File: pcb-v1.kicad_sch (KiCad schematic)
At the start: 0 parts

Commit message: add arduino due symbol
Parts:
- added A1: Arduino_Due_Shield, PCM_arduino-library:Arduino_Due_Shield, symbol arduino-library-wit:Arduino_Due_Shield
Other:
- company: (none) -> Control Data (Thailand) LTD.
- title: (none) -> IOBox

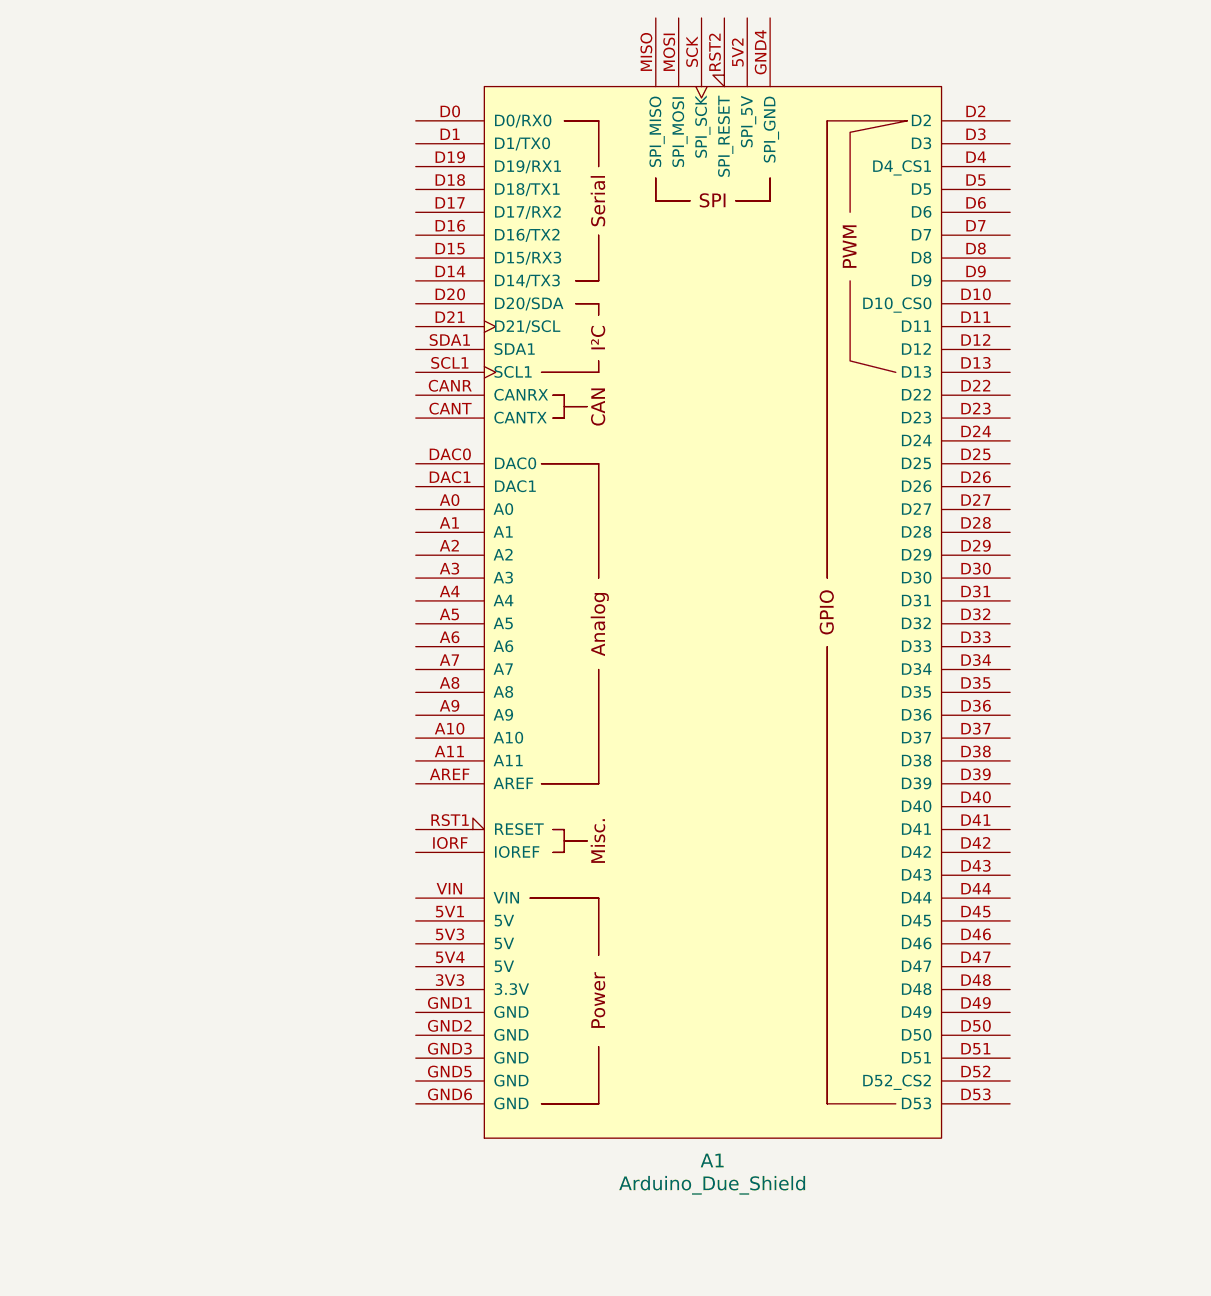
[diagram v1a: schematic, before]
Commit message: add voltage sensor pin
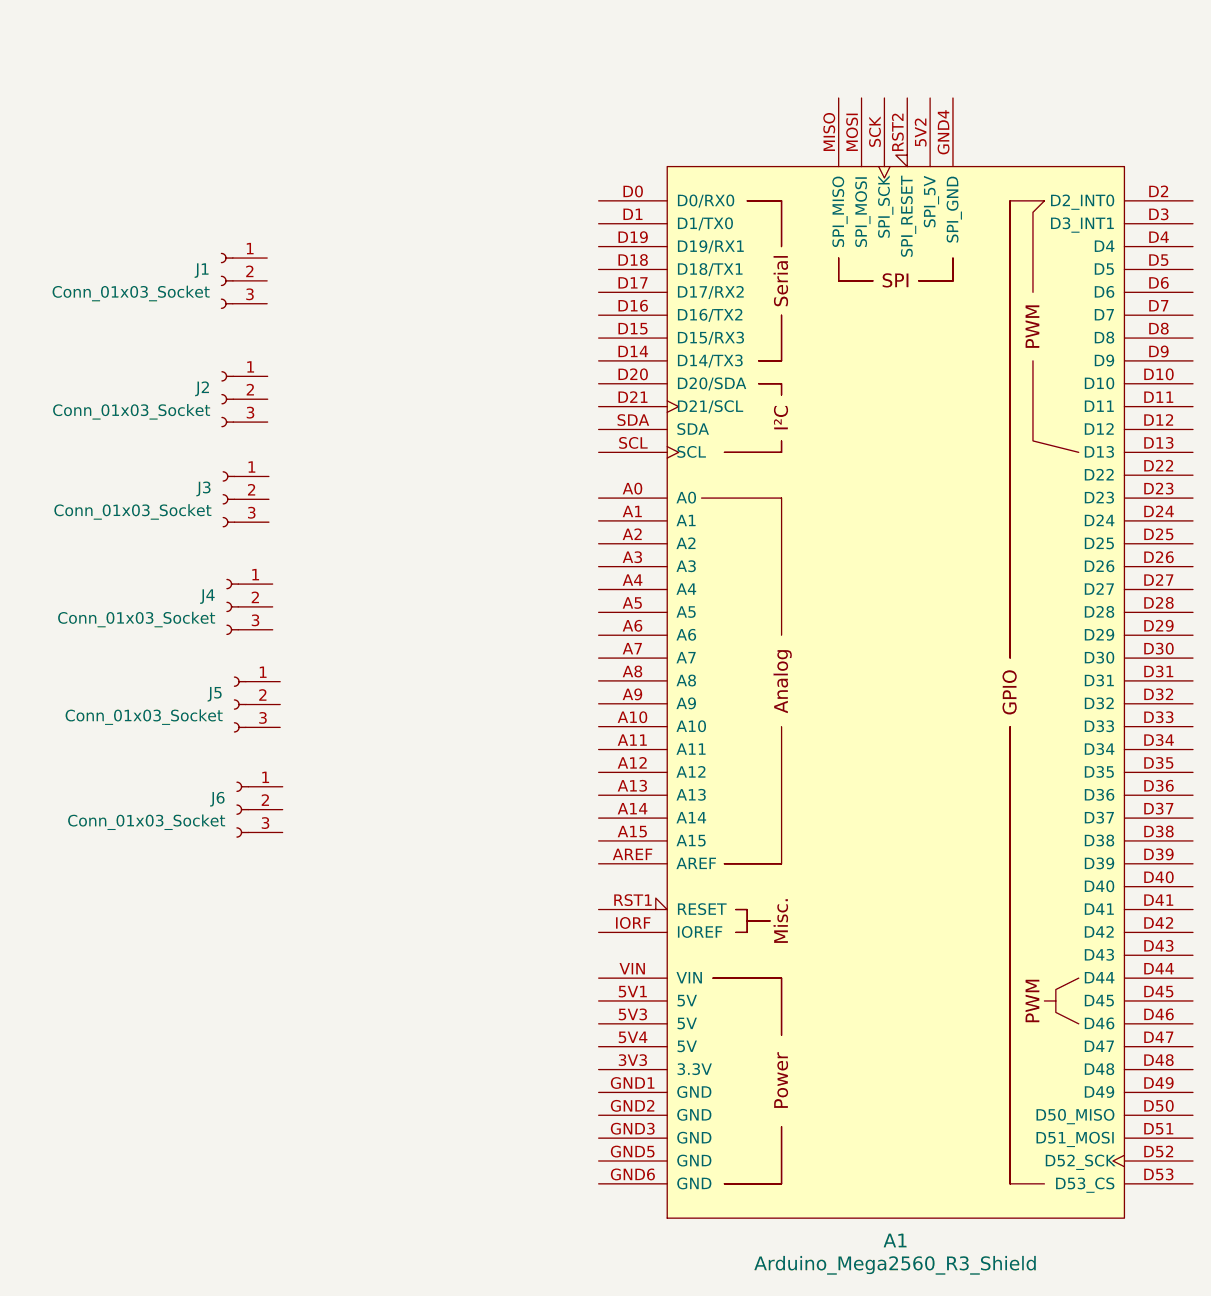
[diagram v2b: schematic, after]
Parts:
- removed A1: Arduino_Due_Shield, PCM_arduino-library:Arduino_Due_Shield, symbol arduino-library-wit:Arduino_Due_Shield
- added A1: Arduino_Mega2560_R3_Shield, arduino-library:Arduino_Mega2560_R3_Shield, symbol arduino-library-kidcad:Arduino_Mega2560_R3_Shield
- added J1, J2, J3, J4, J5, J6: Conn_01x03_Socket, Connector_PinSocket_2.54mm:PinSocket_1x03_P2.54mm_Vertical, symbol Connector:Conn_01x03_Socket

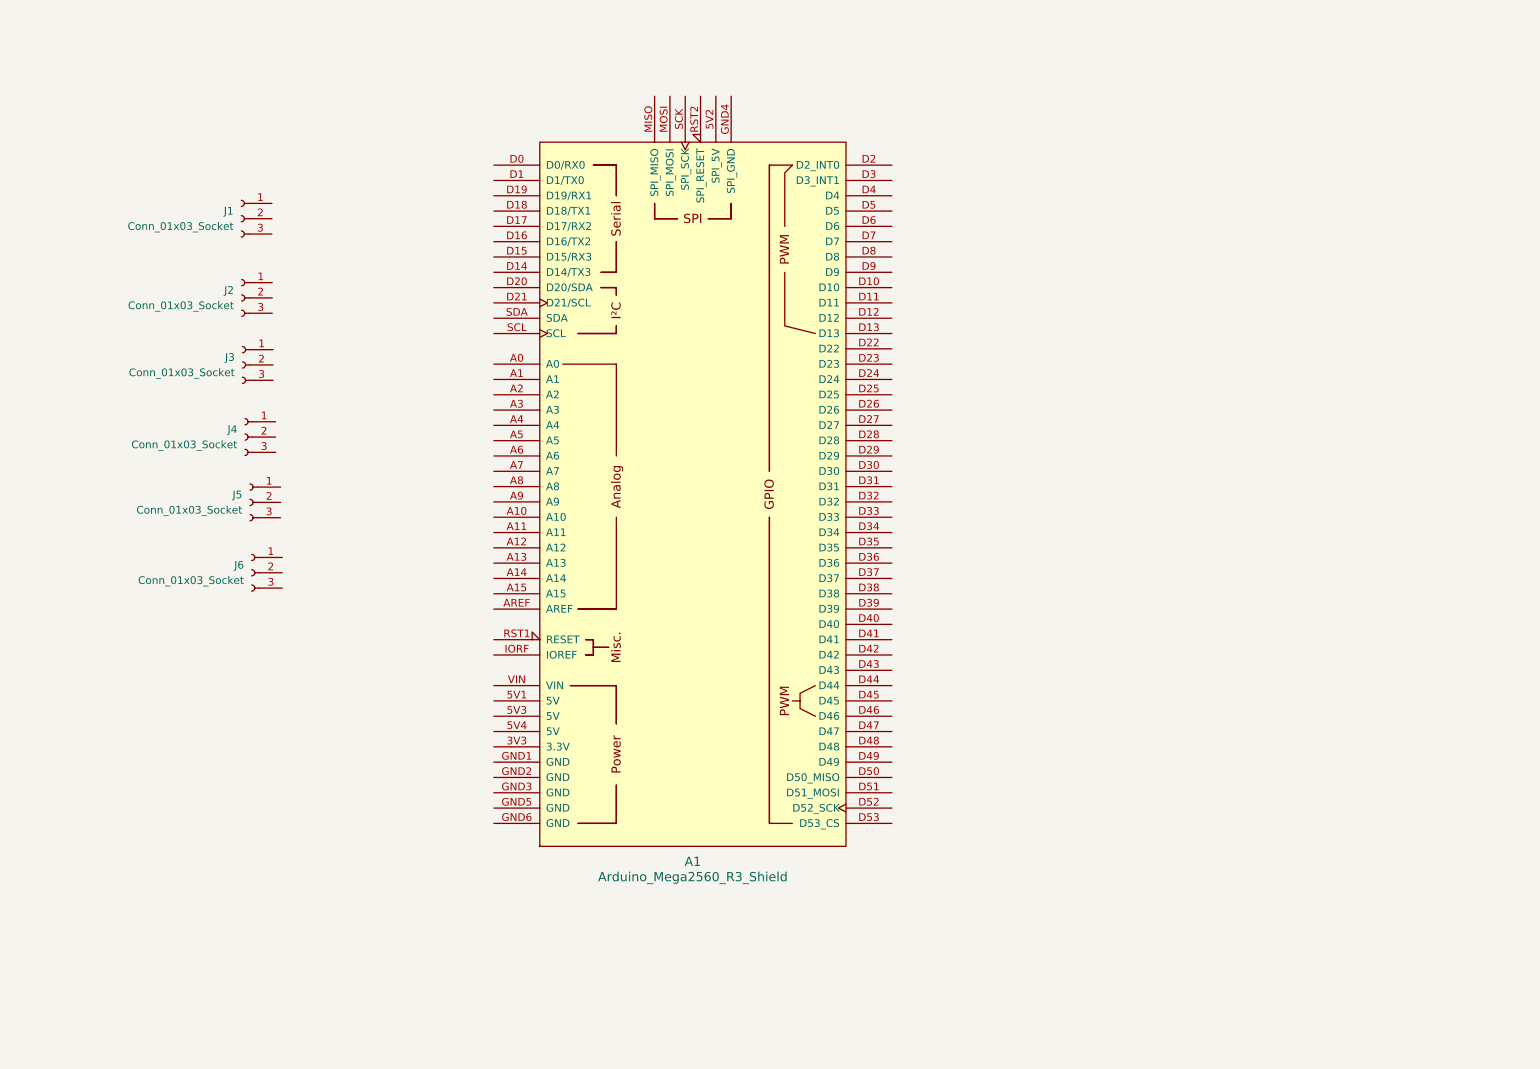
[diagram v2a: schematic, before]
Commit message: add all symbol and footprint
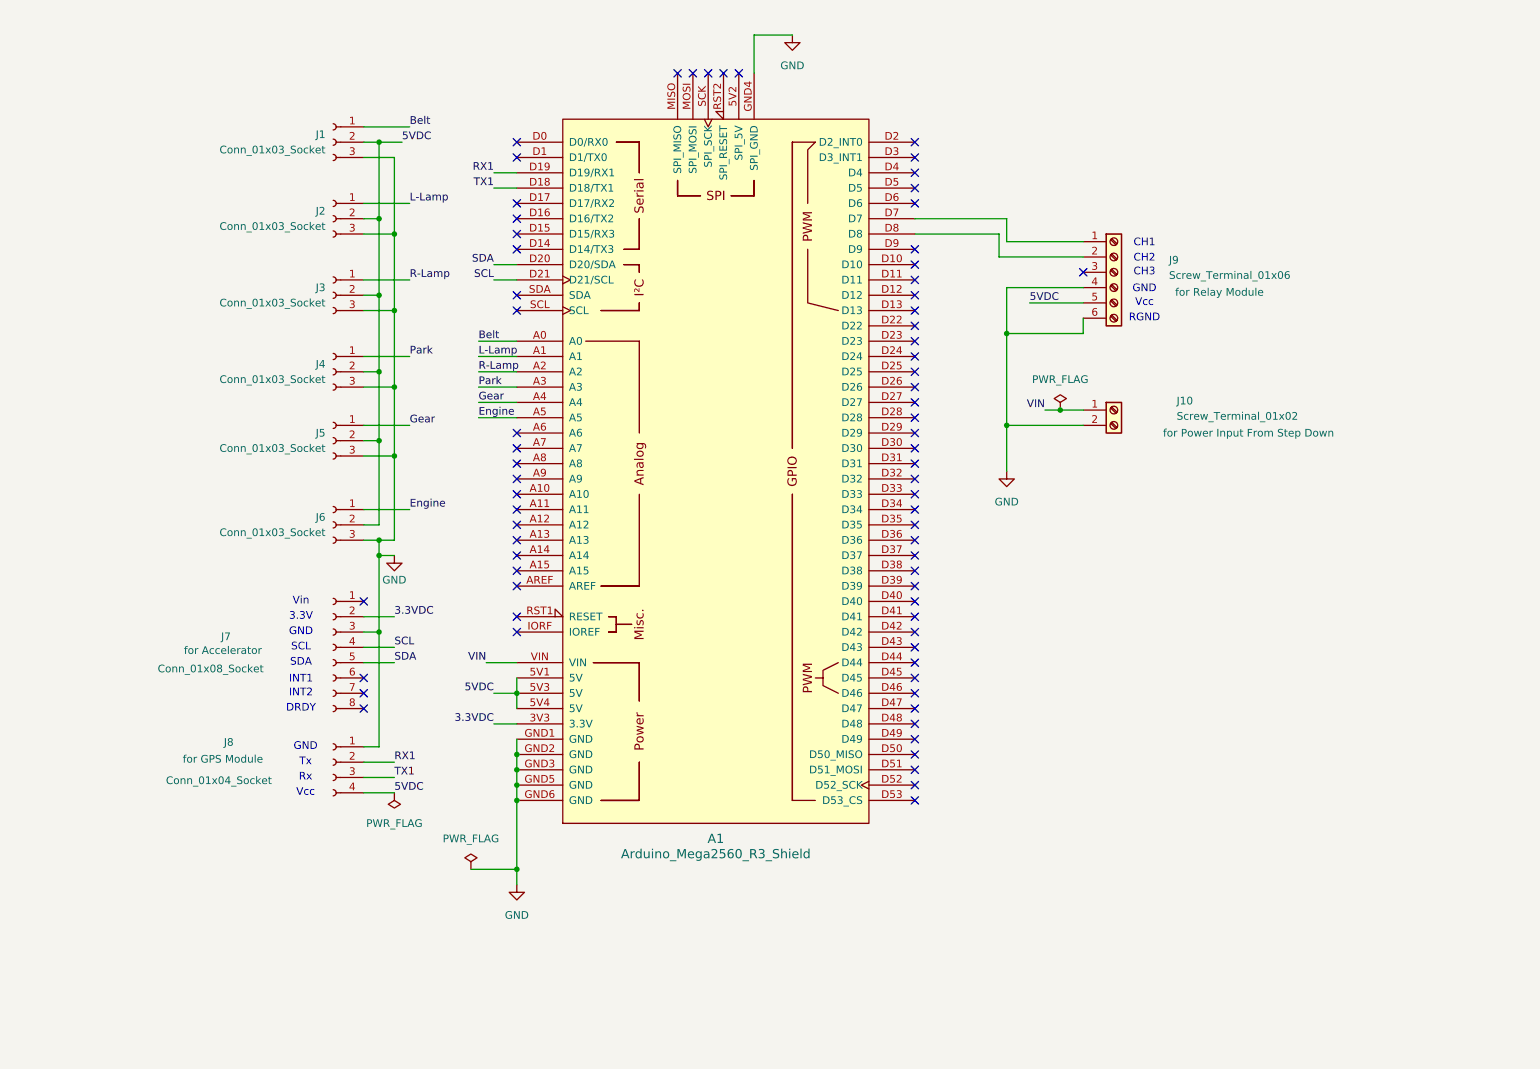
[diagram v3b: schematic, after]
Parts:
- added J10: Screw_Terminal_01x02, TerminalBlock_Phoenix:TerminalBlock_Phoenix_MKDS-3-2-5.08_1x02_P5.08mm_Horizontal, symbol Connector:Screw_Terminal_01x02
- added J7: Conn_01x08_Socket, Connector_PinSocket_2.54mm:PinSocket_1x08_P2.54mm_Vertical, symbol Connector:Conn_01x08_Socket
- added J8: Conn_01x04_Socket, Connector_PinSocket_2.54mm:PinSocket_1x04_P2.54mm_Vertical, symbol Connector:Conn_01x04_Socket
- added J9: Screw_Terminal_01x06, TerminalBlock_Phoenix:TerminalBlock_Phoenix_MKDS-1,5-6-5.08_1x06_P5.08mm_Horizontal, symbol Connector:Screw_Terminal_01x06
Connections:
- net 3.3VDC: now reaches A1.3V3 (3.3V)
- net 3.3VDC: now also J7.2 (Pin_2)
- net 5VDC: now reaches A1.5V1 (5V)
- net 5VDC: now also A1.5V3 (5V), A1.5V4 (5V), J1.2 (Pin_2), J2.2 (Pin_2), J3.2 (Pin_2), J4.2 (Pin_2), J5.2 (Pin_2), J6.2 (Pin_2), J8.4 (Pin_4), J9.5 (Pin_5)
- net Belt: now reaches A1.A0
- net Belt: now also J1.1 (Pin_1)
- net L-Lamp: now reaches A1.A1
- net L-Lamp: now also J2.1 (Pin_1)
- net R-Lamp: now reaches A1.A2
- net R-Lamp: now also J3.1 (Pin_1)
- net Park: now reaches A1.A3
- net Park: now also J4.1 (Pin_1)
- net Gear: now reaches A1.A4
- net Gear: now also J5.1 (Pin_1)
- net Engine: now reaches A1.A5
- net Engine: now also J6.1 (Pin_1)
- net TX1: now reaches A1.D18 (D18/TX1)
- net TX1: now also J8.3 (Pin_3)
- net RX1: now reaches A1.D19 (D19/RX1)
- net RX1: now also J8.2 (Pin_2)
- net SDA: now reaches A1.D20 (D20/SDA)
- net SDA: now also J7.5 (Pin_5)
- net SCL: now reaches A1.D21 (D21/SCL)
- net SCL: now also J7.4 (Pin_4)
- net at A1.D7: now also J9.1 (Pin_1)
- net at A1.D8: now also J9.2 (Pin_2)
- net GND: now reaches A1.GND1 (GND)
- net GND: now also A1.GND2 (GND), A1.GND3 (GND), A1.GND4 (SPI_GND), A1.GND5 (GND), A1.GND6 (GND), J1.3 (Pin_3), J2.3 (Pin_3), J3.3 (Pin_3), J4.3 (Pin_3), J5.3 (Pin_3), J6.3 (Pin_3), J10.2 (Pin_2), J7.3 (Pin_3), J8.1 (Pin_1), J9.4 (Pin_4), J9.6 (Pin_6)
- net VIN: now reaches A1.VIN
- net VIN: now also J10.1 (Pin_1)
- no-connect marks 0 -> 73
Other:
- note added: "3.3V"
- note added: "CH1"
- note added: "CH2"
- note added: "CH3"
- note added: "DRDY"
- note added: "GND"
- note added: "INT1"
- note added: "INT2"
- note added: "RGND"
- note added: "Rx"
- note added: "SCL"
- note added: "SDA"
- note added: "Tx"
- note added: "Vcc"
- note added: "Vin"
- moved on the sheet: A1, J1, J2, J3, J4, J5, J6

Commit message: before routing
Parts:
- removed J9: Screw_Terminal_01x06, TerminalBlock_Phoenix:TerminalBlock_Phoenix_MKDS-1,5-6-5.08_1x06_P5.08mm_Horizontal, symbol Connector:Screw_Terminal_01x06
- added H1, H10, H11, H12, H2, H3, H4, H5, H6, H7, H8, H9: MountingHole, MountingHole:MountingHole_4.5mm, symbol Mechanical:MountingHole
- added J11, J12, J13: Screw_Terminal_01x04, TerminalBlock_Phoenix:TerminalBlock_Phoenix_MKDS-3-4-5.08_1x04_P5.08mm_Horizontal, symbol Connector:Screw_Terminal_01x04
- added J14: Screw_Terminal_01x06, TerminalBlock_Phoenix:TerminalBlock_Phoenix_MKDS-3-6-5.08_1x06_P5.08mm_Horizontal, symbol Connector:Screw_Terminal_01x06
- added J15, J9: Conn_01x06_Pin, Connector_Molex:Molex_KK-396_A-41792-0006_1x06_P3.96mm_Horizontal, symbol Connector:Conn_01x06_Pin
- J1: for equipment? (none) -> Voltage Sensor
- J10: value Screw_Terminal_01x02 -> Screw_Terminal_01x04; footprint TerminalBlock_Phoenix:TerminalBlock_Phoenix_MKDS-3-2-5.08_1x02_P5.08mm_Horizontal -> TerminalBlock_Phoenix:TerminalBlock_Phoenix_MKDS-3-4-5.08_1x04_P5.08mm_Horizontal; symbol Connector:Screw_Terminal_01x02 -> Connector:Screw_Terminal_01x04; for equipment? for Power Input From Step Down -> for Power 7-8V From Step Down
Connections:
- net 5VDC: now also J9.1 (Pin_1)
- net GND: now also J11.1 (Pin_1), J11.2 (Pin_2), J11.3 (Pin_3), J11.4 (Pin_4), J12.1 (Pin_1), J12.2 (Pin_2), J12.3 (Pin_3), J12.4 (Pin_4), J9.2 (Pin_2); no longer J10.2 (Pin_2)
- net VIN: now also J10.2 (Pin_2), J10.3 (Pin_3), J10.4 (Pin_4)
- net at A1.D10: now also J9.6 (Pin_6)
- net at A1.D7: now also J9.3 (Pin_3)
- net at A1.D8: now also J9.4 (Pin_4)
- net at A1.D9: now also J9.5 (Pin_5)
- new net: J14.1 (Pin_1), J15.1 (Pin_1)
- new net: J14.2 (Pin_2), J15.2 (Pin_2)
- new net: J14.3 (Pin_3), J15.3 (Pin_3)
- new net: J14.4 (Pin_4), J15.4 (Pin_4)
- new net: J14.5 (Pin_5), J15.5 (Pin_5)
- new net: J14.6 (Pin_6), J15.6 (Pin_6)
- new net 12VDC: J13.1 (Pin_1), J13.2 (Pin_2), J13.3 (Pin_3), J13.4 (Pin_4)
- no-connect marks 73 -> 70
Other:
- note added: "12V"
- note added: "5V"
- note added: "7-8V"
- note added: "CH4"
- note added: "signal"
- note removed: "RGND"
- moved on the sheet: A1, J1, J2, J3, J4, J5, J6, J7, J8

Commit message: add part finish
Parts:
- added H13, H14, H15, H16: MountingHole, MountingHole:MountingHole_4.5mm, symbol Mechanical:MountingHole
- H1, H2, H3, H4, H5, H6, H7, H8: footprint MountingHole:MountingHole_4.5mm -> MountingHole:MountingHole_3.2mm_M3
- J10: for equipment? for Power 7-8V From Step Down -> Power 7-8V From Step Down
- J11: for equipment? for Power 7-8V From Step Down -> GND From Step Down
- J12: for equipment? for Power 12V From Car Battery -> GND From Car Battery
- J13: for equipment? for Power 12V From Car Battery -> Power 12V From Car Battery
- J2: for equipment? (none) -> L-Lamp
- J3: for equipment? (none) -> R-Lamp
- J4: for equipment? (none) -> Park
- J5: for equipment? (none) -> Gear
- J6: for equipment? (none) -> Engine
